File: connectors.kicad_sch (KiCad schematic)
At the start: 10 parts

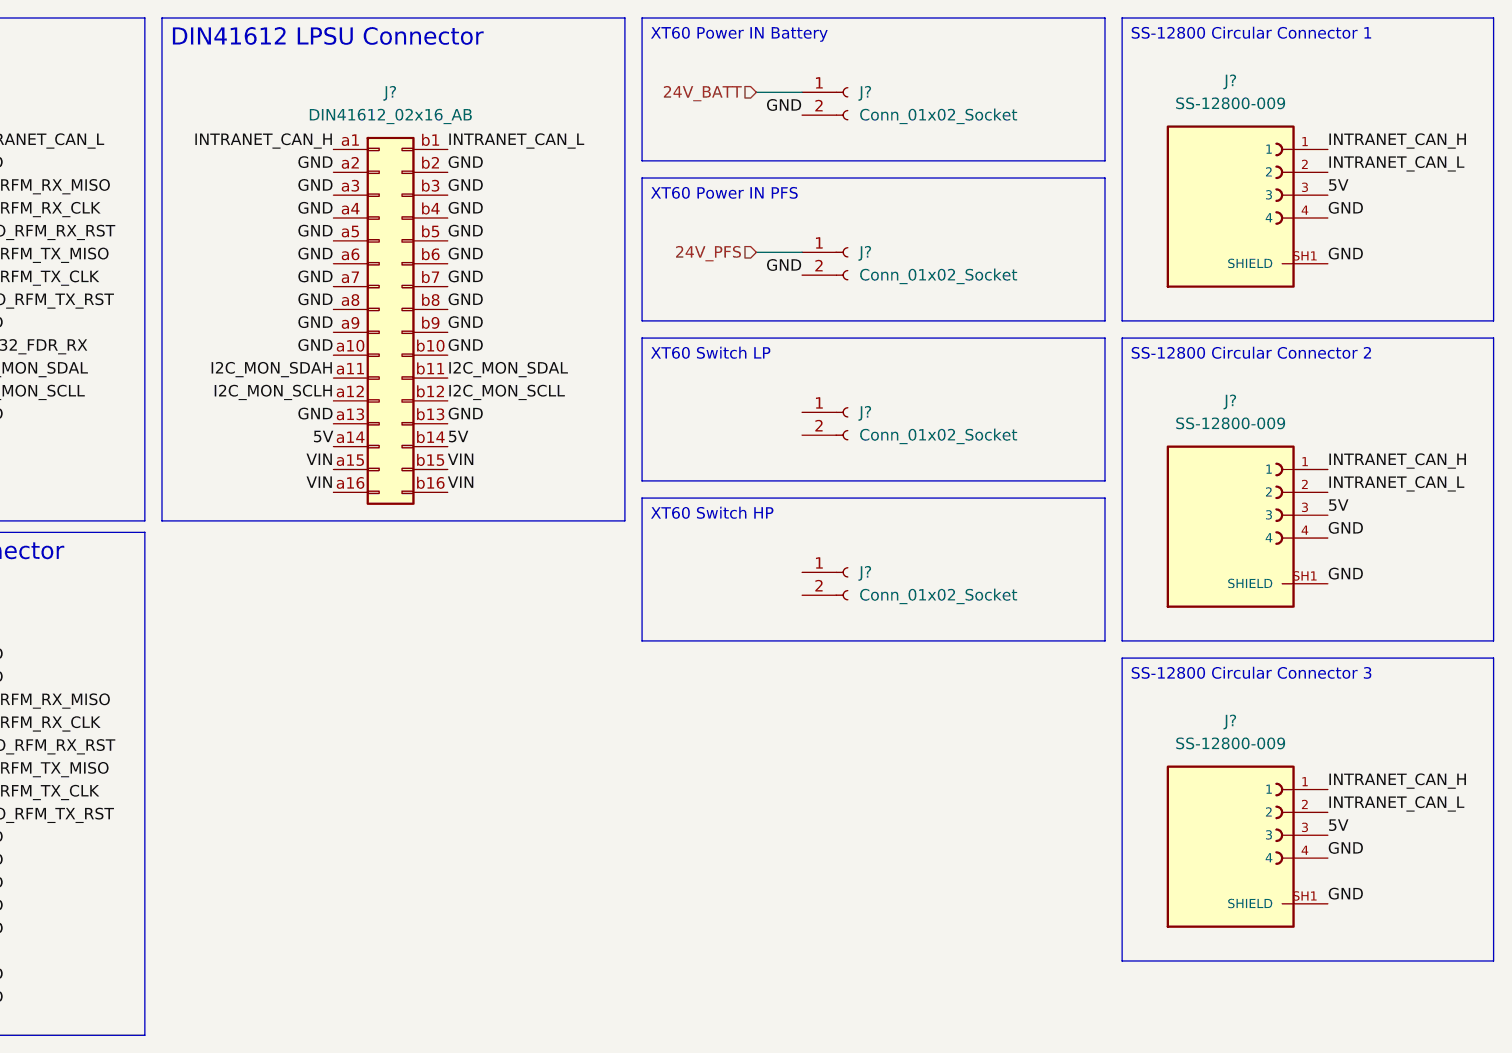
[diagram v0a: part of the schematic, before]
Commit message: add: missing connectors + XT60 switches
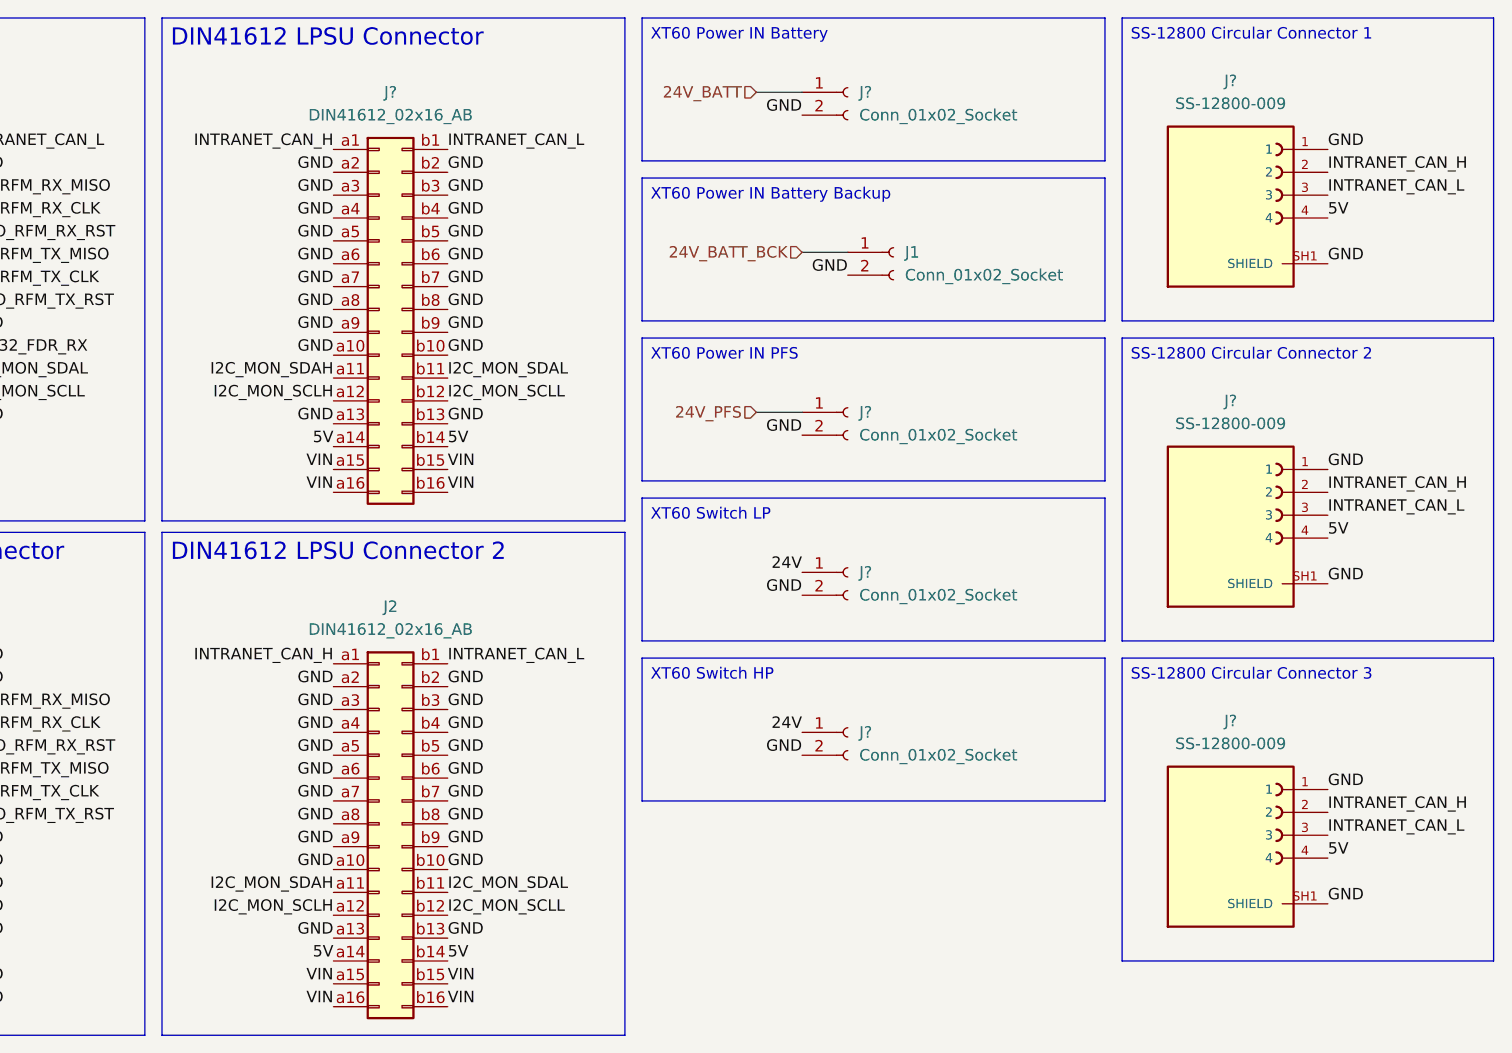
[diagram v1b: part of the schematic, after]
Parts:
- added J1: Conn_01x02_Socket, symbol Connector:Conn_01x02_Socket
- added J2: DIN41612_02x16_AB, symbol Connector:DIN41612_02x16_AB
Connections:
- net 24V: now also J?.1 (Pin_1), J?.1 (Pin_1)
- net 5V: now also J?.4, J?.4, J?.4, J2.a14 (Pin_a14), J2.b14 (Pin_b14); no longer J?.3, J?.3, J?.3
- net GND: now also J?.1, J?.1, J?.1, J?.2 (Pin_2), J?.2 (Pin_2), J1.2 (Pin_2), J2.a10 (Pin_a10), J2.a13 (Pin_a13), J2.a2 (Pin_a2), J2.a3 (Pin_a3), J2.a4 (Pin_a4), J2.a5 (Pin_a5), J2.a6 (Pin_a6), J2.a7 (Pin_a7), J2.a8 (Pin_a8), J2.a9 (Pin_a9), J2.b10 (Pin_b10), J2.b13 (Pin_b13), J2.b2 (Pin_b2), J2.b3 (Pin_b3), J2.b4 (Pin_b4), J2.b5 (Pin_b5), J2.b6 (Pin_b6), J2.b7 (Pin_b7), J2.b8 (Pin_b8), J2.b9 (Pin_b9); no longer J?.4, J?.4, J?.4
- net I2C_MON_SCLH: now also J2.a12 (Pin_a12)
- net I2C_MON_SCLL: now also J2.b12 (Pin_b12)
- net I2C_MON_SDAH: now also J2.a11 (Pin_a11)
- net I2C_MON_SDAL: now also J2.b11 (Pin_b11)
- net INTRANET_CAN_H: now also J?.2, J?.2, J?.2, J2.a1 (Pin_a1); no longer J?.1, J?.1, J?.1
- net INTRANET_CAN_L: now also J?.3, J?.3, J?.3, J2.b1 (Pin_b1); no longer J?.2, J?.2, J?.2
- net VIN: now also J2.a15 (Pin_a15), J2.a16 (Pin_a16), J2.b15 (Pin_b15), J2.b16 (Pin_b16)
- new net 24V_BATT_BCK: J1.1 (Pin_1)
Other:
- moved on the sheet: J?

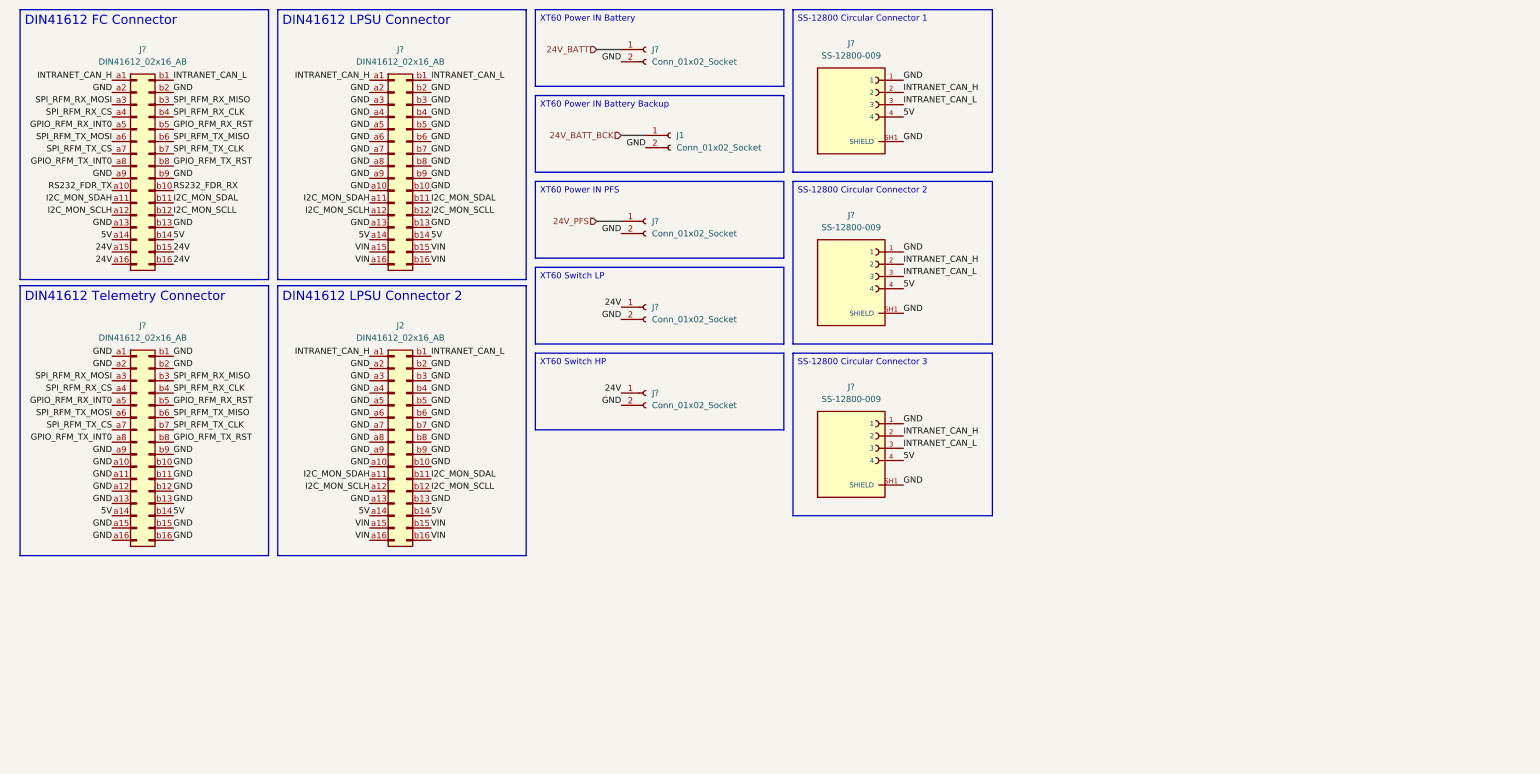
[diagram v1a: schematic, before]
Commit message: add: power MUX + global labels
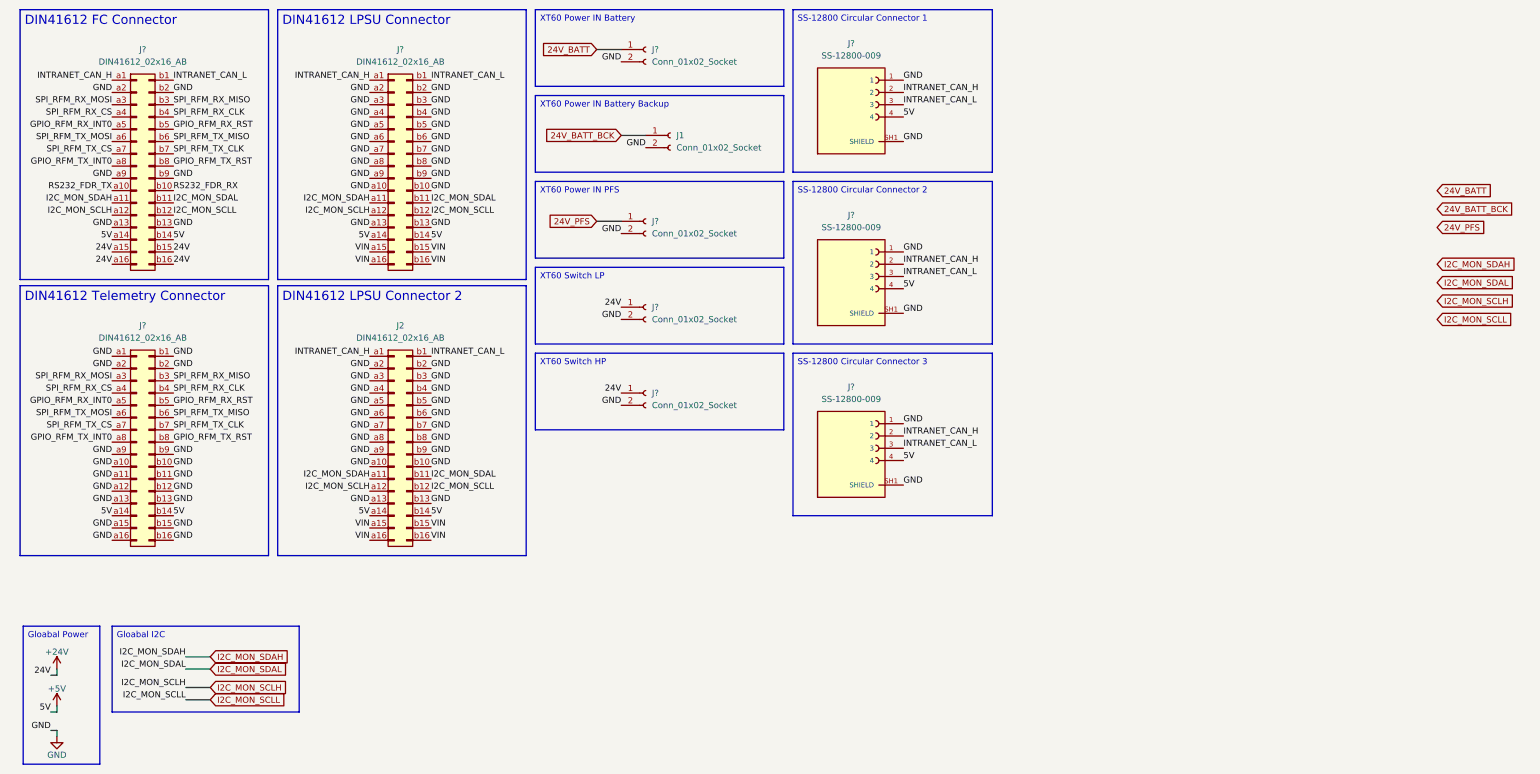
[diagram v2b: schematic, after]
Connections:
- net 24V renamed +24V
- net 5V renamed +5V
